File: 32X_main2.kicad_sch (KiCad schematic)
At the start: 54 parts, among them IC501 SH2 M, IC502 SH2 S, IC503 uPD4502161, IC504 315-5818, IC506 315-5781, IC507 TC511664, IC508 TC511664, IC509 74AC04, IC510 RHSRL33A

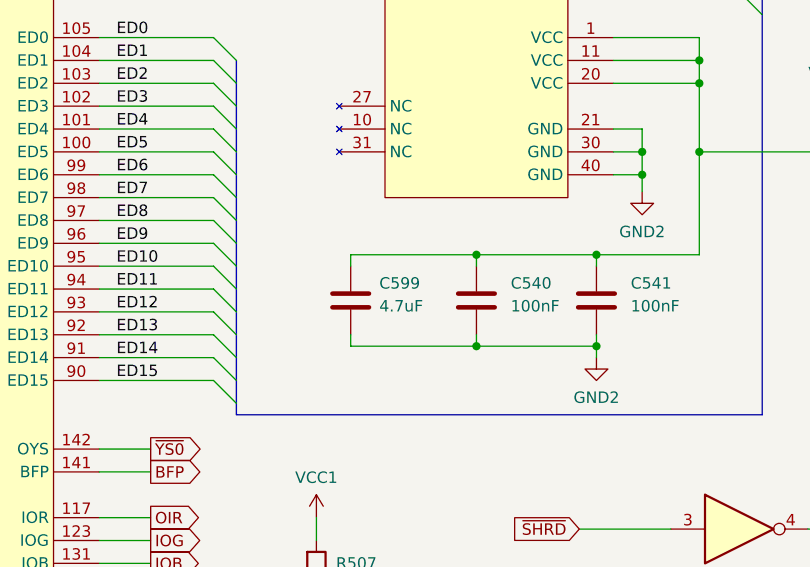
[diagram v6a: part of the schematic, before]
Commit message: More tweaks, documentation. Add hex file for switchless mod.
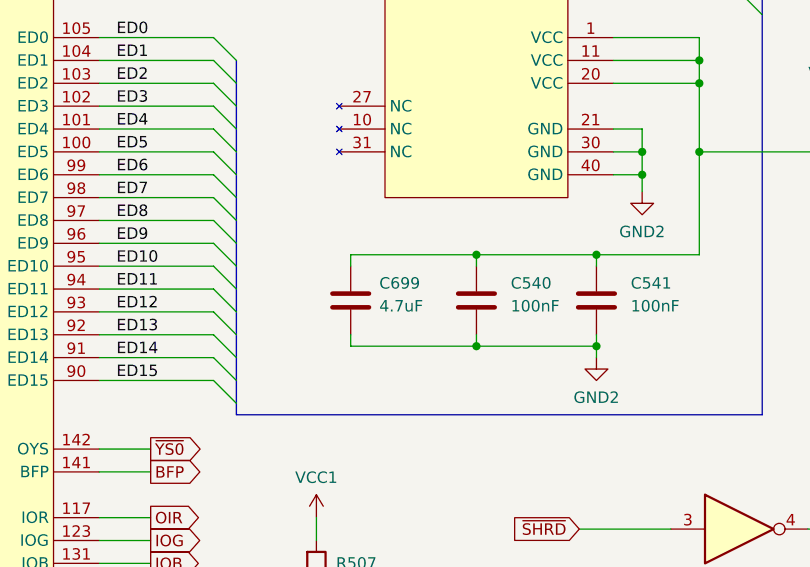
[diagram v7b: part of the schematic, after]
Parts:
- renumbered C599 to C699
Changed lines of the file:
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@@
   (symbol (lib_id "Device:C") (at 297.815 207.01 0) (mirror y) (unit 1)
     (in_bom yes) (on_board yes) (dnp no)
-    (property "Reference" "C599" (at 300.99 205.105 0)
+    (property "Reference" "C699" (at 300.99 205.105 0)
       (effects (font (size 1.27 1.27)) (justify right))
     )
@@
       (project "Neptune"
         (path "/bcc23b51-b742-4ae5-9dd6-d96a24058944/e4c57f96-d802-4292-9df6-7ff62ef14a9e"
-          (reference "C599") (unit 1)
+          (reference "C699") (unit 1)
         )
       )

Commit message: General tweaks, add some DigiKey part numbers.
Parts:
- renumbered C596 to C696, C597 to C697
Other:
- note added: "Description"
- note added: "HD6417095/F23 HD6417095/F28 HD6417095/F28"
- note added: "IC502 Part No."
- note added: "Originally C96 and C97, which are THT capacitors soldered directly to the chips on VA1 main boards. Renumbered 6xx to replace with SMD parts."
- note added: "Value"
- note removed: "C596/C597"
- note removed: "IC2 PART No."
